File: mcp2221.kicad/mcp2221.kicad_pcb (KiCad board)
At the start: 2 copper layers, 47.2 x 32.8 mm, 26 parts, among them J1 Jumper 32 or 21, J2 Conn_01x04_Male, J3 Conn_01x03_Male, J4 Conn_01x06_Male, J5 Conn_01x03_Male, J6 Conn_01x06_Male, J7 Conn_01x02_Male, J8 Conn_01x02_Male, SW1 SW_Push, SW2 SW_Push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

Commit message: fixed labels
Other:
- board text added: "Rev 9"
- board text removed: "Rev 8"
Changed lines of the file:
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@@
     (effects (font (size 0.8 0.8) (thickness 0.15)))
   )
-  (gr_text "Rev 8" (at 67.7926 80.2894) (layer B.SilkS)
+  (gr_text "Rev 9" (at 67.7926 80.2894) (layer B.SilkS)
     (effects (font (size 1 1) (thickness 0.15)) (justify mirror))
   )
@@
   (gr_line (start 79.0448 54.0512) (end 79.0448 56.1086) (layer F.SilkS) (width 0.12))
   (gr_line (start 78.0034 54.0512) (end 79.0448 54.0512) (layer F.SilkS) (width 0.12))
-  (gr_text GND (at 108.6866 68.7832) (layer F.SilkS)
+  (gr_text GND (at 109.1946 66.2686) (layer F.SilkS)
     (effects (font (size 1 1) (thickness 0.15)))
   )
-  (gr_text VDD (at 108.7374 66.2178) (layer F.SilkS)
+  (gr_text VDD (at 109.1946 68.7832) (layer F.SilkS)
     (effects (font (size 1 1) (thickness 0.15)))
   )
-  (gr_text SDA (at 108.7374 63.627) (layer F.SilkS)
+  (gr_text SDA (at 109.0676 61.2648) (layer F.SilkS)
     (effects (font (size 1 1) (thickness 0.15)))
   )
-  (gr_text SCL (at 108.6866 61.1632) (layer F.SilkS)
+  (gr_text SCL (at 109.093 63.7032) (layer F.SilkS)
     (effects (font (size 1 1) (thickness 0.15)))
   )

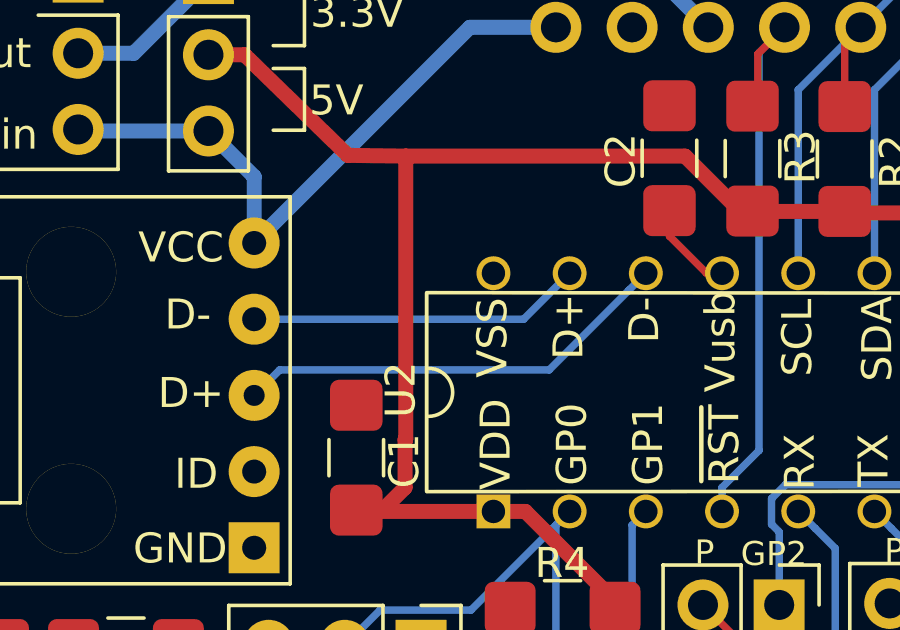
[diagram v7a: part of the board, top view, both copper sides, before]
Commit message: Rev 10: fix order of D-/D+ in schematic+pcb
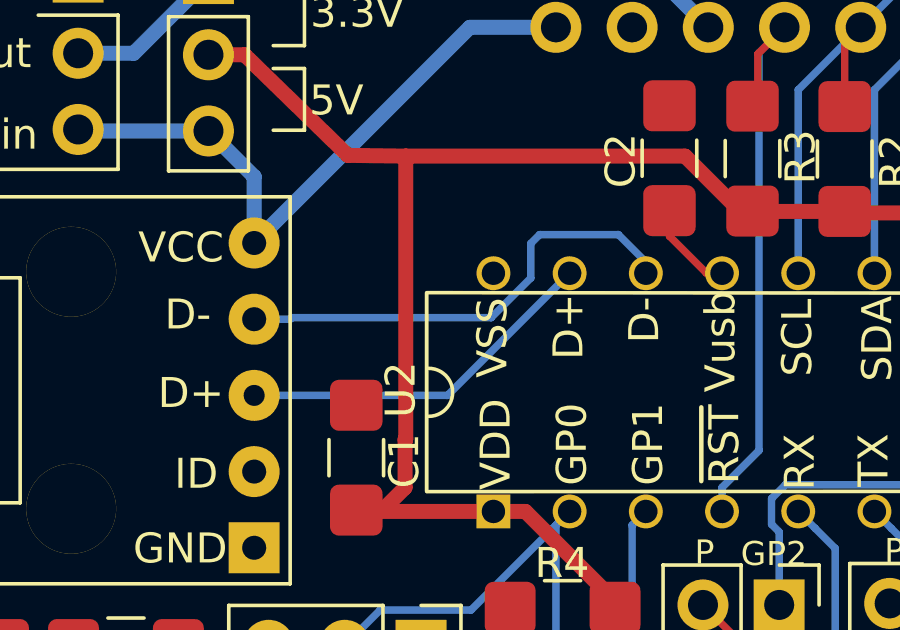
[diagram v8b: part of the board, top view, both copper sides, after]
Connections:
- USB1 pad 3: /USB-D- -> /USB-D+
- USB1 pad 4: /USB-D+ -> /USB-D-
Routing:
- net /USB-D+: track 11.2 -> 12.2 mm
- net /USB-D-: track 14.7 -> 15.6 mm
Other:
- board text added: "GP0: IO, LED-RX GP1: IO, LED-TX, ADC1 GP2: IO, DAC, ADC2 GP3: IO, DAC, ADC3, LED-I2C"
- board text added: "Rev 10"
- board text removed: "GP0: IO, LED-RX GP1: IO, LED-TX, ADC1 GP2: IO, DAC, ADC2 GP3: IO, DAC, ADC3"
- board text removed: "Rev 9"
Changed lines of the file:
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@@
     (thickness 1.6)
     (drawings 44)
-    (tracks 155)
+    (tracks 160)
     (zones 0)
     (modules 26)
@@
       (net 18 /5V))
     (pad 4 thru_hole oval (at 0 7.62 180) (size 1.7 1.7) (drill 0.8) (layers *.Cu *.Mask)
+      (net 15 /USB-D-))
+    (pad 3 thru_hole oval (at 0 5.08 180) (size 1.7 1.7) (drill 0.7) (layers *.Cu *.Mask)
       (net 14 /USB-D+))
-    (pad 3 thru_hole oval (at 0 5.08 180) (size 1.7 1.7) (drill 0.7) (layers *.Cu *.Mask)
-      (net 15 /USB-D-))
     (pad 2 thru_hole oval (at 0 2.54 180) (size 1.7 1.7) (drill 0.8) (layers *.Cu *.Mask)
       (net 16 "Net-(USB1-Pad2)"))
@@
     )
   )
-  (gr_text "GP0: IO, LED-RX\nGP1: IO, LED-TX, ADC1\nGP2: IO, DAC, ADC2\nGP3: IO, DAC, ADC3" (at 102.5906 64.77) (layer B.SilkS)
+  (gr_text "GP0: IO, LED-RX\nGP1: IO, LED-TX, ADC1\nGP2: IO, DAC, ADC2\nGP3: IO, DAC, ADC3, LED-I2C" (at 102.5906 64.77) (layer B.SilkS)
     (effects (font (size 1 1) (thickness 0.15)) (justify left mirror))
   )
@@
     (effects (font (size 0.8 0.8) (thickness 0.15)))
   )
-  (gr_text "Rev 9" (at 67.7926 80.2894) (layer B.SilkS)
+  (gr_text "Rev 10" (at 67.7926 80.2894) (layer B.SilkS)
     (effects (font (size 1 1) (thickness 0.15)) (justify mirror))
   )
@@
   (segment (start 98.044 54.7624) (end 100.1268 52.6796) (width 0.25) (layer B.Cu) (net 13))
   (segment (start 98.044 60.8762) (end 98.044 54.7624) (width 0.25) (layer B.Cu) (net 13))
-  (segment (start 86.3524 62.4078) (end 87.884 60.8762) (width 0.25) (layer B.Cu) (net 14))
-  (segment (start 77.3684 62.4078) (end 86.3524 62.4078) (width 0.25) (layer B.Cu) (net 14))
-  (segment (start 89.859001 61.441199) (end 90.424 60.8762) (width 0.25) (layer B.Cu) (net 15))
-  (segment (start 87.202399 64.097801) (end 89.859001 61.441199) (width 0.25) (layer B.Cu) (net 15))
-  (segment (start 78.218399 64.097801) (end 87.202399 64.097801) (width 0.25) (layer B.Cu) (net 15))
-  (segment (start 77.3684 64.9478) (end 78.218399 64.097801) (width 0.25) (layer B.Cu) (net 15))
+  (segment (start 83.8124 64.9478) (end 87.884 60.8762) (width 0.25) (layer B.Cu) (net 14))
+  (segment (start 77.3684 64.9478) (end 83.8124 64.9478) (width 0.25) (layer B.Cu) (net 14))
+  (segment (start 86.8858 59.5884) (end 89.5096 59.5884) (width 0.25) (layer B.Cu) (net 15))
+  (segment (start 78.570481 62.4078) (end 78.621281 62.357) (width 0.25) (layer B.Cu) (net 15))
+  (segment (start 77.3684 62.4078) (end 78.570481 62.4078) (width 0.25) (layer B.Cu) (net 15))
+  (segment (start 86.5886 59.8856) (end 86.8858 59.5884) (width 0.25) (layer B.Cu) (net 15))
+  (segment (start 78.621281 62.357) (end 85.2678 62.357) (width 0.25) (layer B.Cu) (net 15))
+  (segment (start 85.2678 62.357) (end 86.5886 61.0362) (width 0.25) (layer B.Cu) (net 15))
+  (segment (start 86.5886 61.0362) (end 86.5886 59.8856) (width 0.25) (layer B.Cu) (net 15))
+  (segment (start 90.424 60.5028) (end 90.424 60.833) (width 0.25) (layer B.Cu) (net 15))
+  (segment (start 89.5096 59.5884) (end 90.424 60.5028) (width 0.25) (layer B.Cu) (net 15))
   (segment (start 73.3552 53.5432) (end 75.8444 51.054) (width 0.5) (layer B.Cu) (net 17))
   (segment (start 71.501 53.5432) (end 73.3552 53.5432) (width 0.5) (layer B.Cu) (net 17))
